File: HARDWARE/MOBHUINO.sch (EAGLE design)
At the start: 28 parts, among them IC1 7805T, IC2 MEGA328-P, Q1 16 MHz, U1 ARDUINO_SHIELDNO_SILK, X2 USB

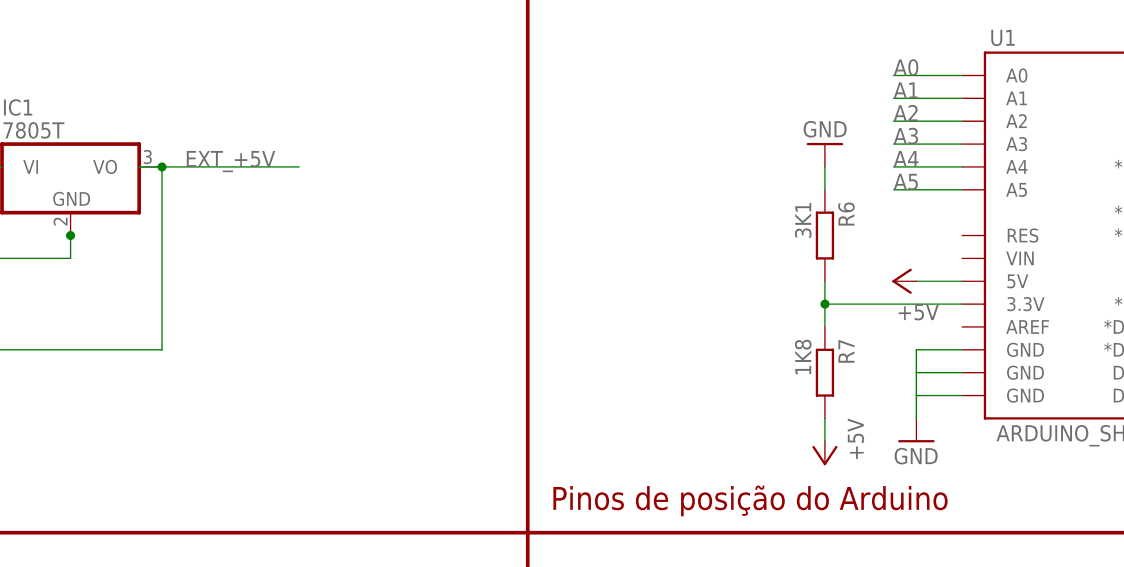
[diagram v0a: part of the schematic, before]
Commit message: - Inserção da malha de terra - Melhorado algumas trilhas - Modificado a linha de corte externa mais para mais grossa
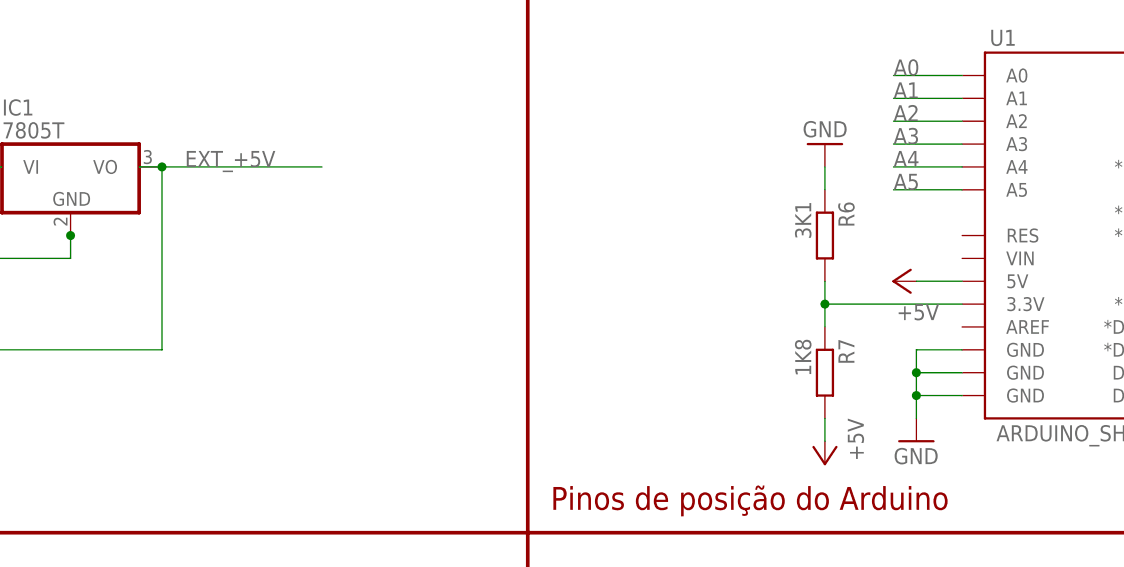
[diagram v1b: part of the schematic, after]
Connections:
- removed net N$24: IC1.VO, JP2.1
- net EXT_+5V: now also IC1.VO, JP2.1
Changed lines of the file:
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@@
 <segment>
 <wire x1="22.86" y1="71.12" x2="22.86" y2="96.52" width="0.1524" layer="91"/>
-<wire x1="40.64" y1="96.52" x2="22.86" y2="96.52" width="0.1524" layer="91"/>
 <wire x1="22.86" y1="71.12" x2="38.1" y2="71.12" width="0.1524" layer="91"/>
 <wire x1="38.1" y1="71.12" x2="40.64" y2="71.12" width="0.1524" layer="91"/>
 <wire x1="38.1" y1="66.04" x2="38.1" y2="71.12" width="0.1524" layer="91"/>
-<junction x="22.86" y="96.52"/>
 <junction x="38.1" y="71.12"/>
-<pinref part="IC2" gate="G$1" pin="AVCC"/>
 <pinref part="GND3" gate="1" pin="+5V"/>
 <pinref part="IC2" gate="G$1" pin="VCC@1"/>
 <pinref part="C3" gate="G$1" pin="2"/>
 <wire x1="22.86" y1="96.52" x2="20.32" y2="96.52" width="0.1524" layer="91"/>
+<pinref part="IC2" gate="G$1" pin="AVCC"/>
+<wire x1="40.64" y1="96.52" x2="22.86" y2="96.52" width="0.1524" layer="91"/>
+<junction x="22.86" y="96.52"/>
 </segment>
 <segment>
@@
 <pinref part="U1" gate="G$1" pin="GND@2"/>
 <wire x1="177.8" y1="144.78" x2="172.72" y2="144.78" width="0.1524" layer="91"/>
+<pinref part="GND4" gate="1" pin="GND"/>
 <wire x1="172.72" y1="144.78" x2="172.72" y2="142.24" width="0.1524" layer="91"/>
-<pinref part="GND4" gate="1" pin="GND"/>
-<pinref part="U1" gate="G$1" pin="GND@0"/>
+<pinref part="U1" gate="G$1" pin="GND@1"/>
 <wire x1="172.72" y1="142.24" x2="172.72" y2="139.7" width="0.1524" layer="91"/>
 <wire x1="172.72" y1="139.7" x2="172.72" y2="137.16" width="0.1524" layer="91"/>
-<wire x1="172.72" y1="139.7" x2="177.8" y2="139.7" width="0.1524" layer="91"/>
-<pinref part="U1" gate="G$1" pin="GND@1"/>
 <wire x1="177.8" y1="142.24" x2="172.72" y2="142.24" width="0.1524" layer="91"/>
+<junction x="172.72" y="142.24"/>
+<pinref part="U1" gate="G$1" pin="GND@0"/>
+<wire x1="177.8" y1="139.7" x2="172.72" y2="139.7" width="0.1524" layer="91"/>
+<junction x="172.72" y="139.7"/>
 </segment>
 <segment>
@@
 <pinref part="R6" gate="G$1" pin="1"/>
 <wire x1="162.56" y1="165.1" x2="162.56" y2="162.56" width="0.1524" layer="91"/>
-</segment>
-</net>
-<net name="N$24" class="0">
-<segment>
-<wire x1="88.9" y1="144.78" x2="88.9" y2="165.1" width="0.1524" layer="91"/>
-<wire x1="88.9" y1="165.1" x2="86.36" y2="165.1" width="0.1524" layer="91"/>
-<pinref part="IC1" gate="A1" pin="VO"/>
-<junction x="88.9" y="165.1"/>
-<wire x1="45.72" y1="144.78" x2="88.9" y2="144.78" width="0.1524" layer="91"/>
-<pinref part="JP2" gate="A" pin="1"/>
 </segment>
 </net>
@@
 <net name="EXT_+5V" class="0">
 <segment>
-<wire x1="88.9" y1="165.1" x2="104.14" y2="165.1" width="0.1524" layer="91"/>
+<wire x1="88.9" y1="165.1" x2="106.68" y2="165.1" width="0.1524" layer="91"/>
 <label x="91.44" y="165.1" size="1.778" layer="95"/>
+<wire x1="88.9" y1="144.78" x2="88.9" y2="165.1" width="0.1524" layer="91"/>
+<wire x1="88.9" y1="165.1" x2="86.36" y2="165.1" width="0.1524" layer="91"/>
+<pinref part="IC1" gate="A1" pin="VO"/>
+<junction x="88.9" y="165.1"/>
+<wire x1="45.72" y1="144.78" x2="88.9" y2="144.78" width="0.1524" layer="91"/>
+<pinref part="JP2" gate="A" pin="1"/>
 </segment>
 <segment>
@@
 </sheet>
 </sheets>
-<errors>
-</errors>
 </schematic>
 </drawing>

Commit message: - Atualizado a data de atualização do circuito
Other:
- note added: "Atualizado: 06/04/2017"
- note removed: "Atualizado: 26/10/2016"
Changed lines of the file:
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@@
 <text x="239.32" y="6.67" size="2.54" layer="94">3.1v</text>
 <text x="207.21" y="29.34" size="1.9304" layer="94">Criado: 26/09/2015</text>
-<text x="207.21" y="24.26" size="1.9304" layer="94">Atualizado: 26/10/2016</text>
+<text x="207.21" y="24.26" size="1.9304" layer="94">Atualizado: 06/04/2017</text>
 <wire x1="248.92" y1="35.56" x2="129.54" y2="35.56" width="0.4064" layer="94"/>
 <wire x1="129.54" y1="35.56" x2="73.66" y2="35.56" width="0.4064" layer="94"/>
